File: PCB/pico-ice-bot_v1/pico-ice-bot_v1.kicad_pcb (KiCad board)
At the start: 2 copper layers, 1 part

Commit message: updated some files
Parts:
- added J1: Mot1, Connector_PinSocket_2.54mm:PinSocket_1x06_P2.54mm_Vertical, F.Cu at (171.2, 55.3)
- added J2: Mot2, Connector_PinSocket_2.54mm:PinSocket_1x06_P2.54mm_Vertical, F.Cu at (151.9, 55.5)
- added J3: Conn_01x04_Socket, Connector_PinHeader_2.54mm:PinHeader_1x04_P2.54mm_Vertical, F.Cu at (167.2, 76.9)
- added R1: KDV12FR180ET, Resistor_SMD:R_1206_3216Metric_Pad1.30x1.75mm_HandSolder, F.Cu at (166.2, 46.0)
- added R2: KDV12FR180ET, Resistor_SMD:R_1206_3216Metric_Pad1.30x1.75mm_HandSolder, F.Cu at (157.1, 46.0)
- added R3: R_US, Resistor_SMD:R_0603_1608Metric_Pad0.98x0.95mm_HandSolder, F.Cu at (168.1, 58.7)
- added R4: R_US, Resistor_SMD:R_0603_1608Metric_Pad0.98x0.95mm_HandSolder, F.Cu at (176.4, 76.7)
- added R5: R_US, Resistor_SMD:R_0603_1608Metric_Pad0.98x0.95mm_HandSolder, F.Cu at (176.4, 79.7)
- added RN1: 742X083101JP, Resistor_SMD:R_Array_Concave_4x0603, F.Cu at (146.7, 59.7)
- added U2: DRV8411RTER, DRV8411:QFN50P300X300X80-17N-D, F.Cu at (161.7, 49.2)
- moved U1 45.6 mm to (162.8, 65.3)
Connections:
- U1 pad 10: unconnected-(U1-ICE38-Pad10) -> /enc2_b
- U1 pad 11: unconnected-(U1-ICE42-Pad11) -> /mot_sleep
- U1 pad 12: unconnected-(U1-ICE43-Pad12) -> /mot_fault
- U1 pad 17: unconnected-(U1-ICE44-Pad17) -> /mot1_a
- U1 pad 18: unconnected-(U1-ICE45-Pad18) -> /mot1_b
- U1 pad 19: unconnected-(U1-ICE46-Pad19) -> /mot2_b
- U1 pad 20: unconnected-(U1-ICE47-Pad20) -> /mot2_a
- U1 pad 21: unconnected-(U1-ICE48-Pad21) -> Net-(RN1-R1.2)
- U1 pad 22: unconnected-(U1-ICE2-Pad22) -> Net-(RN1-R2.2)
- U1 pad 23: unconnected-(U1-ICE3-Pad23) -> Net-(RN1-R3.2)
- U1 pad 24: unconnected-(U1-ICE4-Pad24) -> Net-(RN1-R4.2)
- U1 pad 5: unconnected-(U1-ICE28-Pad5) -> /us_trig
- U1 pad 6: unconnected-(U1-ICE31-Pad6) -> /us_echo
- U1 pad 7: unconnected-(U1-ICE32-Pad7) -> /enc1_a
- U1 pad 8: unconnected-(U1-ICE34-Pad8) -> /enc1_b
- U1 pad 9: unconnected-(U1-ICE36-Pad9) -> /enc2_a
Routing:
- net /mot_fault: track 0.00 -> 45.2 mm, vias 0 -> 1
- net /mot1_b: track 0.00 -> 29.0 mm
- net /mot2_a: track 0.00 -> 26.1 mm
- net /mot1_a: track 0.00 -> 25.6 mm
- net /mot2_b: track 0.00 -> 21.2 mm
- net /mot_sleep: track 0.00 -> 17.5 mm
- net GND: vias 0 -> 15

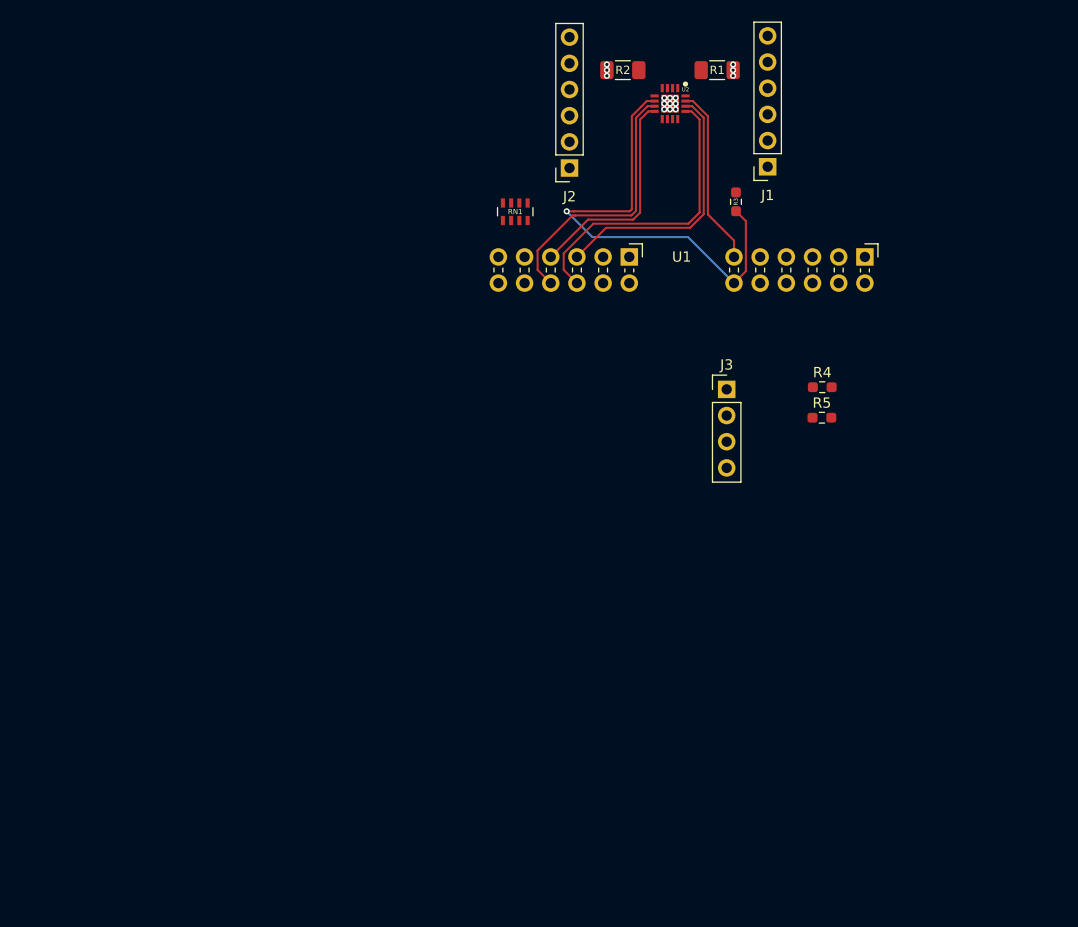
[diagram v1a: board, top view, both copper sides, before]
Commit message: updated schematic and PCB Added batteries, power regulation
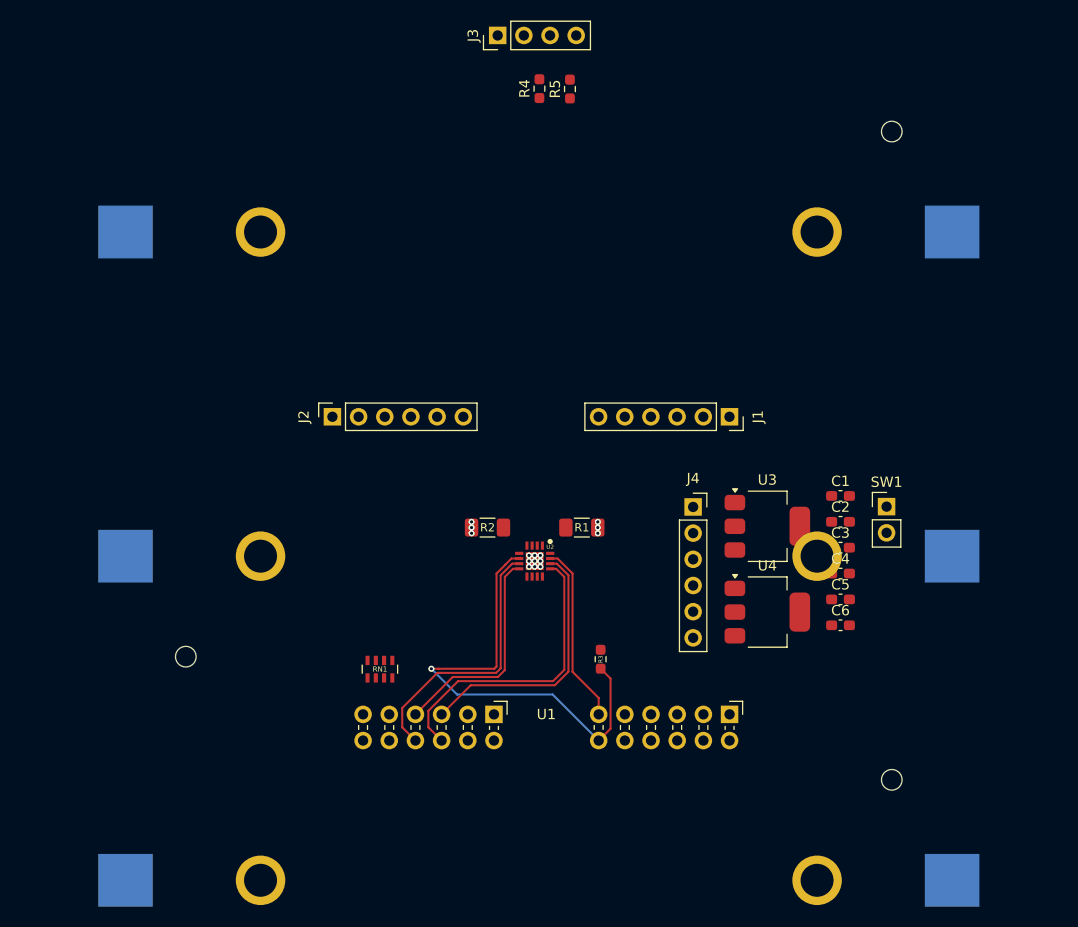
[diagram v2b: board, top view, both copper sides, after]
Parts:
- added B1: 12BHC186P1-GR, Batteries:12BHC186P1GR, B.Cu at (148.9, 124.6)
- added B2: 12BHC186P1-GR, Batteries:12BHC186P1GR, B.Cu at (148.9, 61.7)
- added B3: 12BHC186P1-GR, Batteries:12BHC186P1GR, B.Cu at (148.9, 93.1)
- added C1: CL10A106MA8NRNC, Capacitor_SMD:C_0603_1608Metric_Pad1.08x0.95mm_HandSolder, F.Cu at (178.2, 87.3)
- added C2: 06035G104ZAT2A, Capacitor_SMD:C_0603_1608Metric_Pad1.08x0.95mm_HandSolder, F.Cu at (178.2, 89.8)
- added C3: 06035G104ZAT2A, Capacitor_SMD:C_0603_1608Metric_Pad1.08x0.95mm_HandSolder, F.Cu at (178.2, 92.3)
- added C4: CL10A106MA8NRNC, Capacitor_SMD:C_0603_1608Metric_Pad1.08x0.95mm_HandSolder, F.Cu at (178.2, 94.8)
- added C5: 06035G104ZAT2A, Capacitor_SMD:C_0603_1608Metric_Pad1.08x0.95mm_HandSolder, F.Cu at (178.2, 97.3)
- added C6: CL10A106MA8NRNC, Capacitor_SMD:C_0603_1608Metric_Pad1.08x0.95mm_HandSolder, F.Cu at (178.2, 99.8)
- added J4: PMOD, Connector_PinSocket_2.54mm:PinSocket_1x06_P2.54mm_Vertical, F.Cu at (163.9, 88.3)
- added SW1: 2M1-T2-3, Connector_PinHeader_2.54mm:PinHeader_1x02_P2.54mm_Vertical, F.Cu at (182.7, 88.3)
- added U3: LD1117S50TR_SOT223, Package_TO_SOT_SMD:SOT-223-3_TabPin2, F.Cu at (171.1, 90.2)
- added U4: LD1117S33TR_SOT223, Package_TO_SOT_SMD:SOT-223-3_TabPin2, F.Cu at (171.1, 98.5)
- moved U2 46.3 mm to (148.5, 93.6)
- moved RN1 46.3 mm to (133.5, 104.1)
- moved U1 46.3 mm to (149.7, 109.7)
- moved R1 46.3 mm to (153.1, 90.3)
- moved R2 46.3 mm to (144.0, 90.3)
- moved R3 46.3 mm to (154.9, 103.1)
- moved J3 40.9 mm to (145.0, 42.6), turned to 90 degrees
- moved R5 40.2 mm to (152.0, 47.8), turned to 90 degrees
- moved R4 39.9 mm to (149.0, 47.7), turned to 90 degrees
- moved J2 33.3 mm to (128.9, 79.6), turned to 90 degrees
- moved J1 24.5 mm to (167.4, 79.6), turned to -90 degrees
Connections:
- RN1 pad 1: unconnected-(RN1-R1.1-Pad1) -> /ICE48
- RN1 pad 2: unconnected-(RN1-R2.1-Pad2) -> /ICE2
- RN1 pad 3: unconnected-(RN1-R3.1-Pad3) -> /ICE3
- RN1 pad 4: unconnected-(RN1-R4.1-Pad4) -> /ICE4

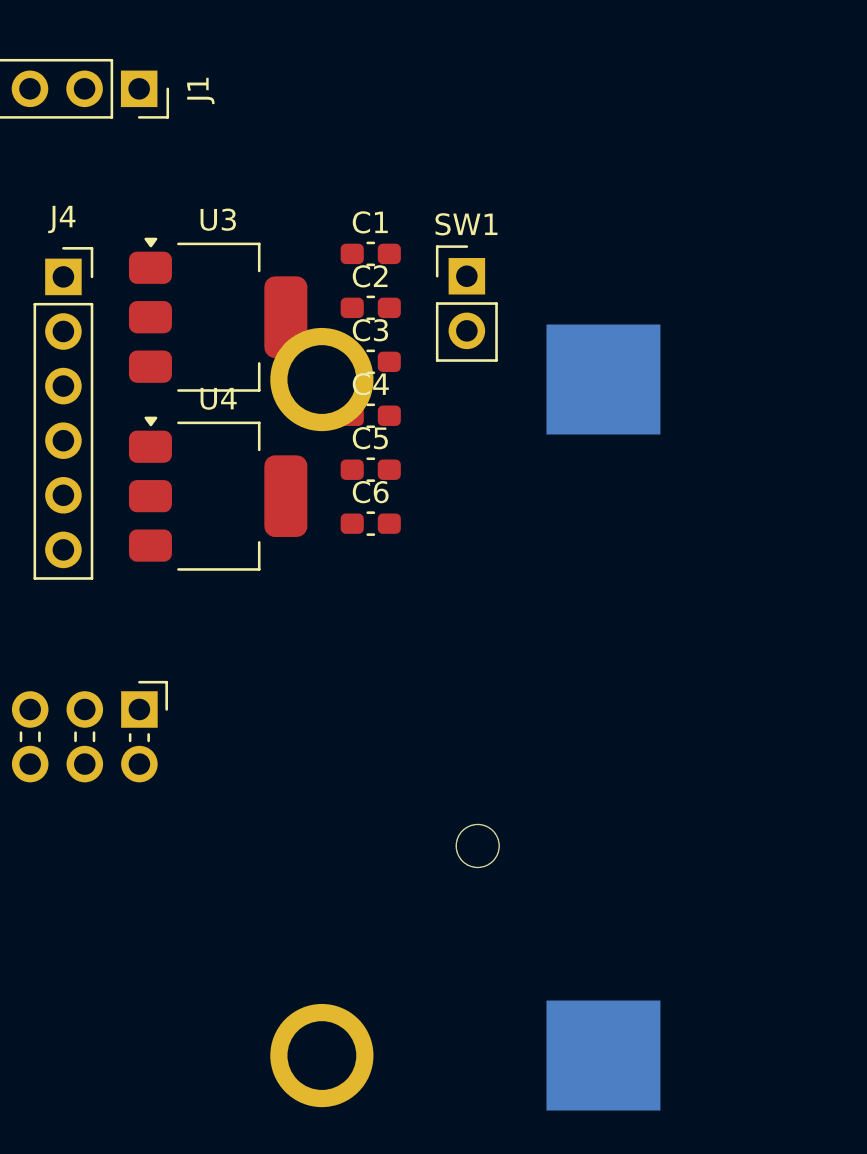
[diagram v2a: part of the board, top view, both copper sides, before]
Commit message: update title block and adjust component positions in PCB and schematic files
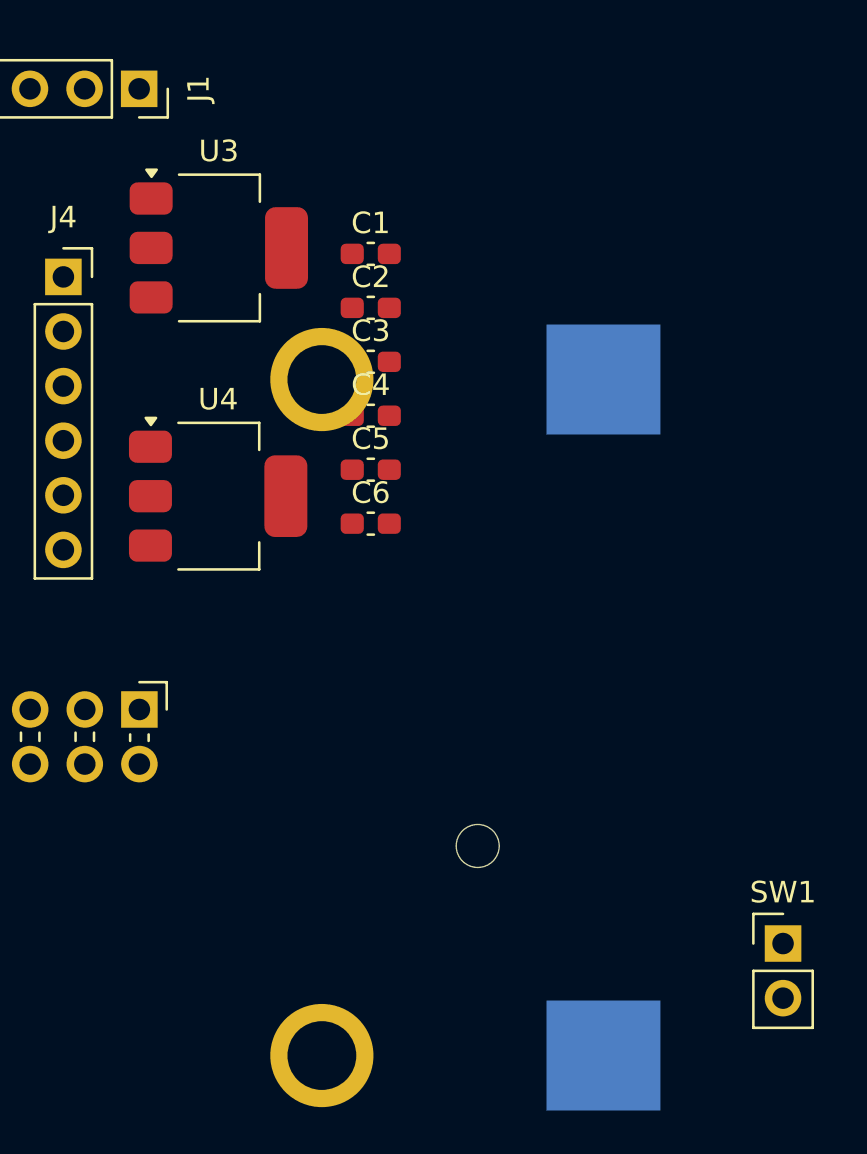
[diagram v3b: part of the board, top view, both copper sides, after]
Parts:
- moved SW1 34.4 mm to (197.4, 119.3)
- moved U3 3.22 mm to (171.2, 87.0)
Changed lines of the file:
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@@
 	(footprint "Package_TO_SOT_SMD:SOT-223-3_TabPin2"
 		(layer "F.Cu")
-		(at 171.12 90.21)
+		(at 171.15 86.9875)
 		(descr "module CMS SOT223 4 pins")
 		(tags "CMS SOT")
@@
 	(footprint "Connector_PinHeader_2.54mm:PinHeader_1x02_P2.54mm_Vertical"
 		(layer "F.Cu")
-		(at 182.69 88.305)
+		(at 197.4 119.35)
 		(descr "Through hole straight pin header, 1x02, 2.54mm pitch, single row")
 		(tags "Through hole pin header THT 1x02 2.54mm single row")
